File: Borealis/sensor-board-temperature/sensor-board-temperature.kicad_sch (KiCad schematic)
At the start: 5 parts, among them J2 Conn_01x03_Pin (data connecti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, J5 Conn_01x03_Pin (power connect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

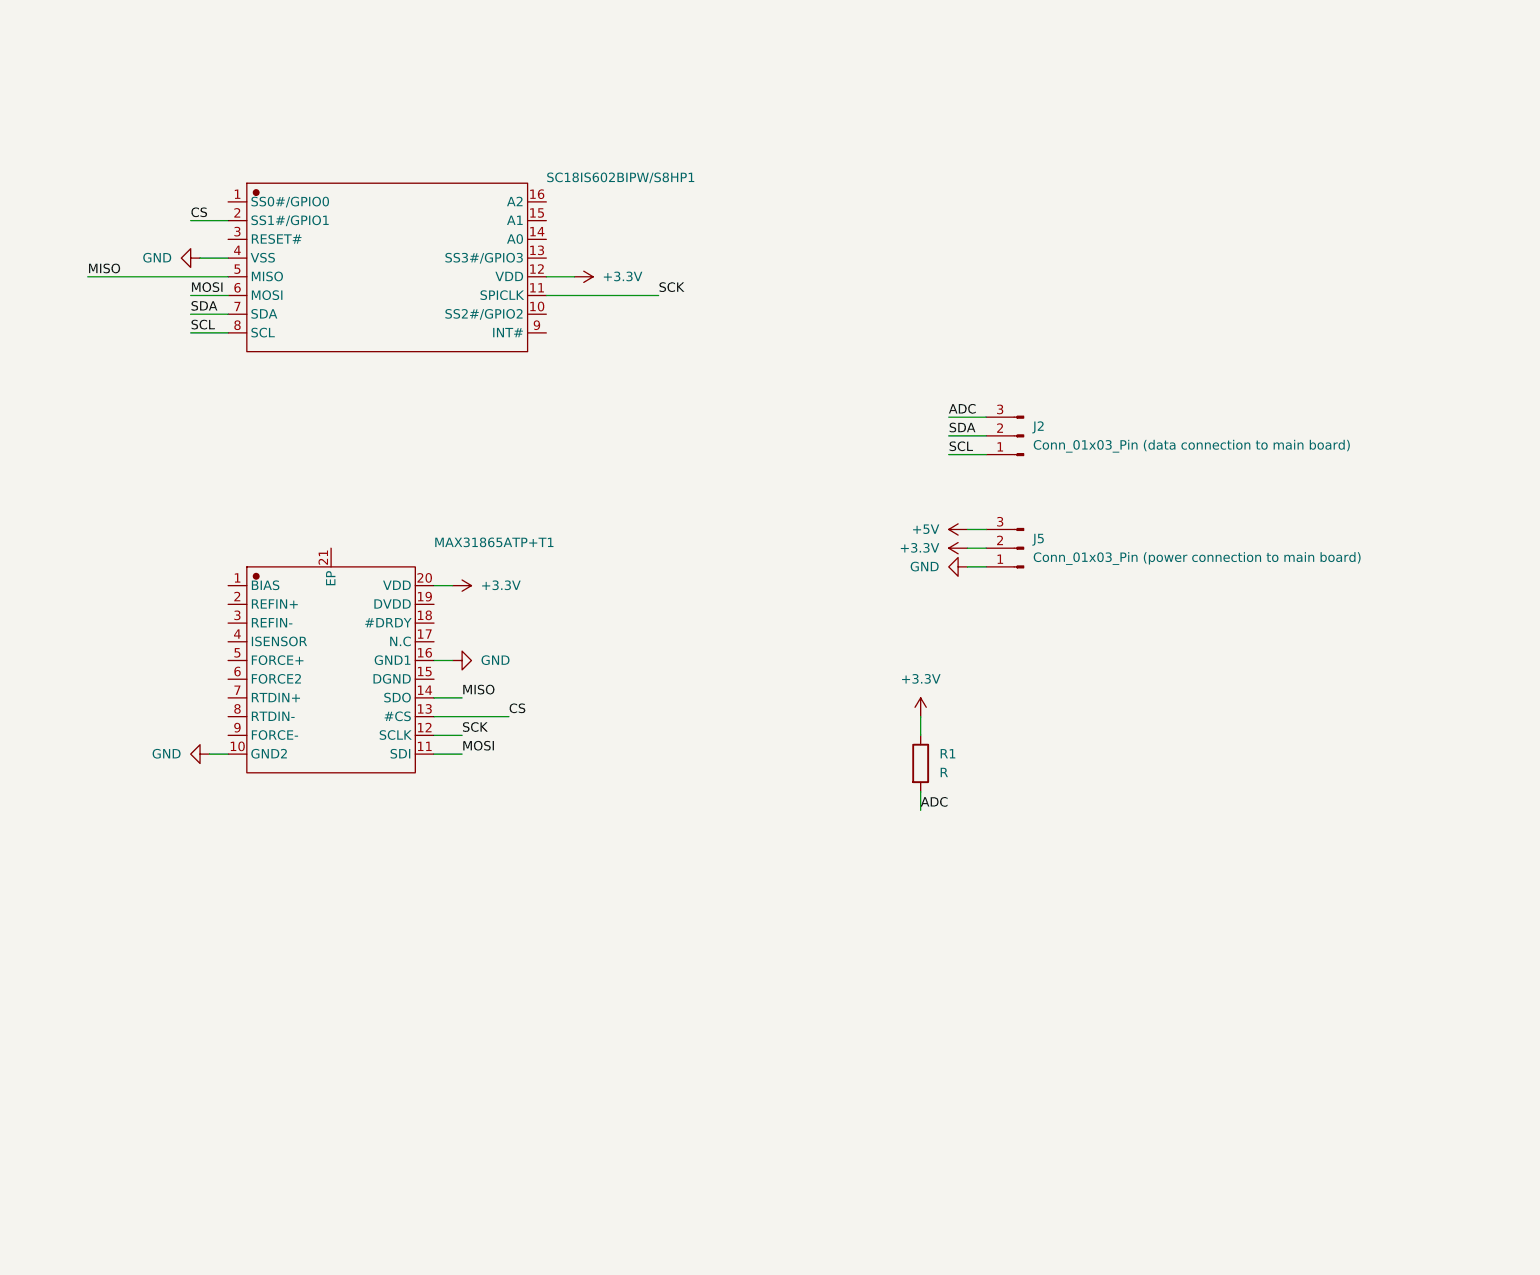
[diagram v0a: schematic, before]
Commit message: Added mainboard and temerature board
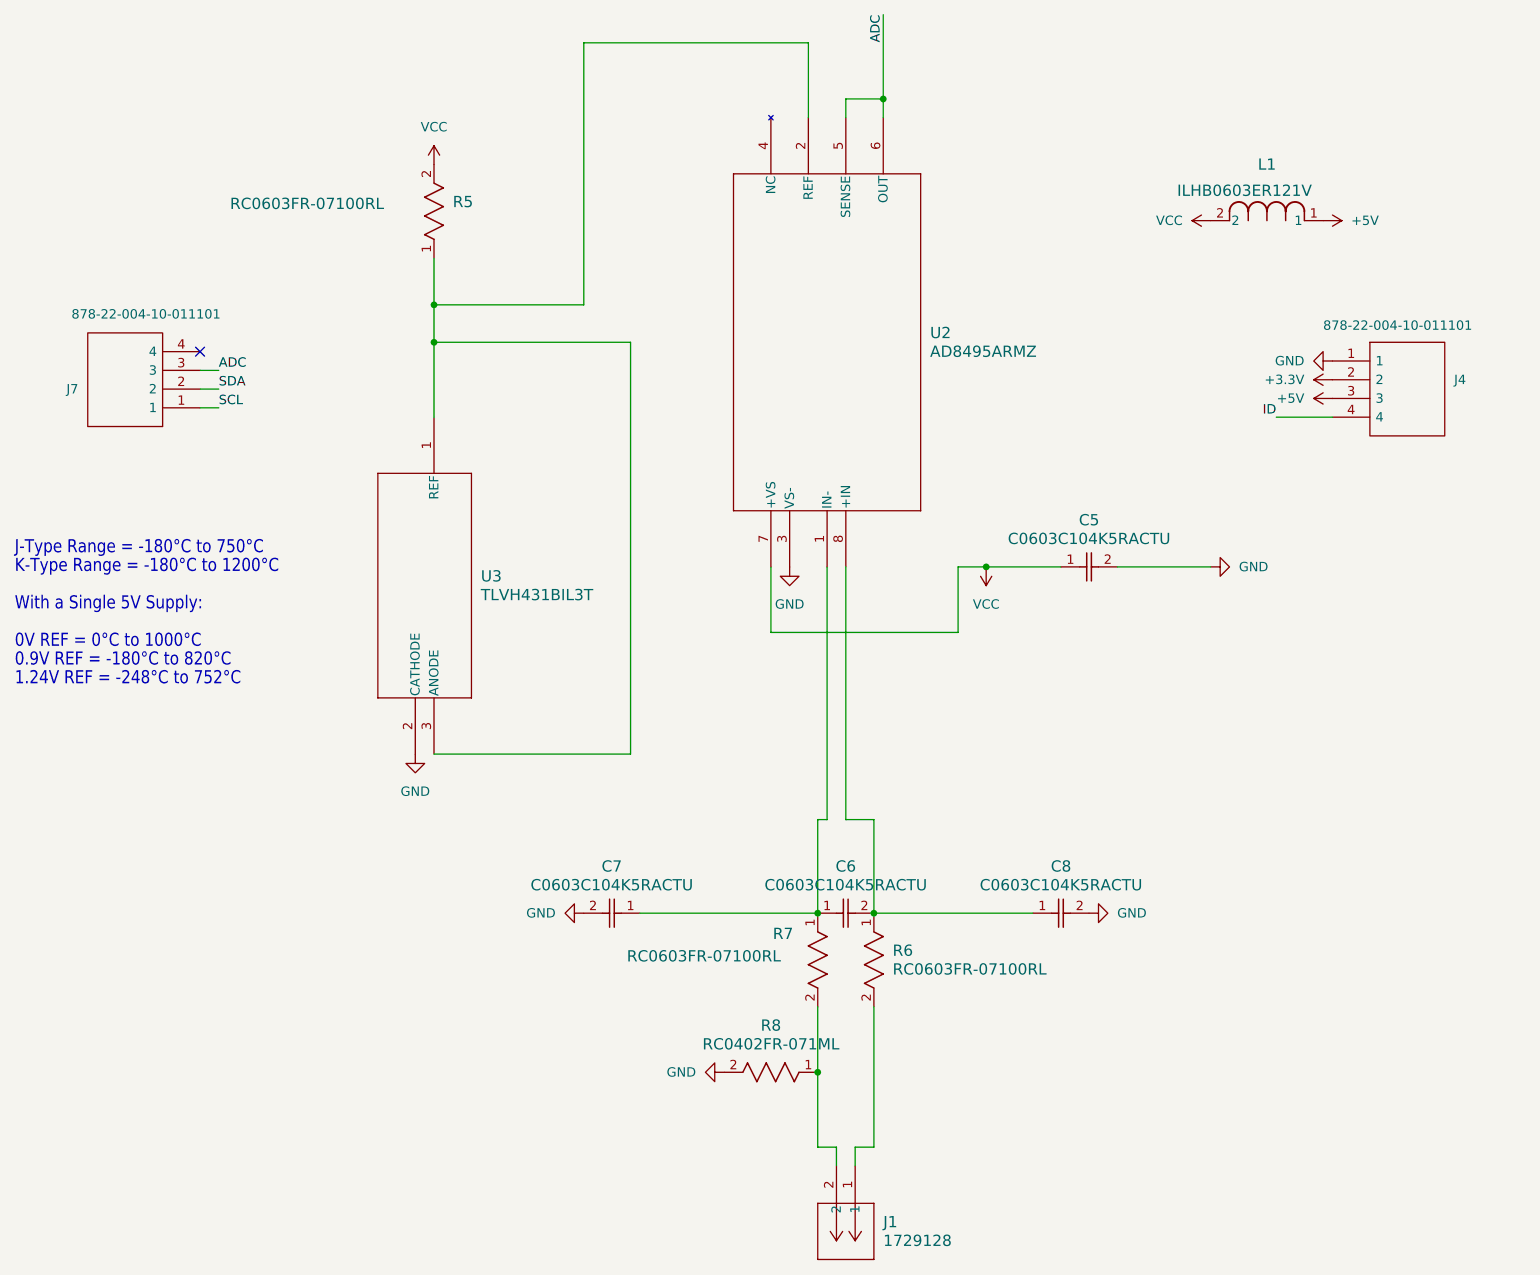
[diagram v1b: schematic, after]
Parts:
- removed J2: Conn_01x03_Pin (data connection to main board), batteryholder:1x03 2.3 pitch, symbol Connector:Conn_01x03_Pin
- removed J5: Conn_01x03_Pin (power connection to main board), batteryholder:1x03 2.3 pitch, symbol Connector:Conn_01x03_Pin
- removed MAX31865ATP+T1: ~, batteryholder:MAX31865ATP+T, symbol MAX31865ATP+T_2025-12-27-altium-import:root_0_MAX31865ATP+T_
- removed R1: R, Resistor_SMD:R_0805_2012Metric, symbol Device:R
- removed SC18IS602BIPW/S8HP1: ~, batteryholder:SC18IS602BIPWS8HP, symbol SC18IS602BIPW-S8HP_2025-12-27-altium-import:root_0_SC18IS602BIPW/S8HP_
- added C5, C6, C7, C8: C0603C104K5RACTU, BOREALIS:CAPC17595_95N_KEM, symbol 2026-01-23_05-30-51:C0603C104K5RACTU
- added J1: 1729128, BOREALIS:CONN_1729128_PXC, symbol 2026-01-23_05-01-15:1729128
- added J4, J7: 878-22-004-10-011101, BOREALIS:8782200410011101, symbol 878-22-004-10-011101:878-22-004-10-011101
- added L1: ILHB0603ER121V, BOREALIS:IND_VISHAY_ILHB0603_VIS, symbol 2026-01-23_05-01-38:ILHB0603ER121V
- added R5, R6, R7: RC0603FR-07100RL, BOREALIS:RC0603N_YAG, symbol 2026-01-23_05-40-00:RC0603FR-07100RL
- added R8: RC0402FR-071ML, BOREALIS:RC0402N_YAG, symbol 2026-01-23_05-51-13:RC0402FR-071ML
- added U2: AD8495ARMZ, BOREALIS:RM_8_ADI, symbol 2026-01-23_05-00-35:AD8495ARMZ
- added U3: TLVH431BIL3T, BOREALIS:SOT23-3-L_3p04x1p4x1p9_STM, symbol 2026-01-23_05-01-00:TLVH431BIL3T
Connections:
- net +3.3V: now also J4.2
- net +5V: now also J4.3, L1.1
- net ADC: now also J7.3, U2.5 (SENSE), U2.6 (OUT)
- net GND: now also C5.2, C7.2, C8.2, J4.1, R8.2, U2.3 (VS-), U3.2 (CATHODE)
- net SCL: now also J7.1
- net SDA: now also J7.2
- new net: R5.1, U2.2 (REF), U3.1 (REF), U3.3 (ANODE)
- new net: C6.1, C7.1, R7.1, U2.1 (IN-)
- new net: C6.2, C8.1, R6.1, U2.8 (+IN)
- new net: J1.2, R7.2, R8.1
- new net: J1.1, R6.2
- new net ID: J4.4
- new net VCC: C5.1, L1.2, R5.2, U2.7 (+VS)
- no-connect marks 0 -> 1
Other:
- note added: "0.9V REF = -180°C to 820°C"
- note added: "0V REF = 0°C to 1000°C"
- note added: "1.24V REF = -248°C to 752°C"
- note added: "J-Type Range = -180°C to 750°C"
- note added: "K-Type Range = -180°C to 1200°C"
- note added: "With a Single 5V Supply:"

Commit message: Fixed a few things
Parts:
- added R1: R, Resistor_SMD:R_0805_2012Metric, symbol Device:R
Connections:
- net +3.3V: now also R1.1
- net ID: now also R1.2
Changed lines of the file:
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@@
+	(wire
+		(pts
+			(xy 212.09 109.22) (xy 212.09 106.68)
+		)
+		(stroke
+			(width 0)
+			(type default)
+		)
+	)
+	(wire
+		(pts
+			(xy 212.09 96.52) (xy 212.09 99.06)
+		)
+		(stroke
+			(width 0)
+			(type default)
+		)
+	)
 	(wire
 		(pts
@@
 		)
 	)
+	(label "ID"
+		(at 212.09 109.22 0)
+		(effects
+			(font
+				(size 1.27 1.27)
+			)
+			(justify left bottom)
+		)
+	)
 	(symbol
 		(lib_id "power:GND")
@@
 	)
 	(symbol
+		(lib_id "power:+3.3V")
+		(at 212.09 96.52 0)
+		(unit 1)
+		(exclude_from_sim no)
+		(in_bom yes)
+		(on_board yes)
+		(dnp no)
+		(fields_autoplaced yes)
+		(property "Reference" "#PWR013"
+			(at 212.09 100.33 0)
+			(effects
+				(font
+					(size 1.27 1.27)
+				)
+				(hide yes)
+			)
+		)
+		(property "Value" "+3.3V"
+			(at 212.09 91.44 0)
+			(effects
+				(font
+					(size 1.27 1.27)
+				)
+			)
+		)
+		(property "Footprint" ""
+			(at 212.09 96.52 0)
+			(effects
+				(font
+					(size 1.27 1.27)
+				)
+				(hide yes)
+			)
+		)
+		(property "Datasheet" ""
+			(at 212.09 96.52 0)
+			(effects
+				(font
+					(size 1.27 1.27)
+				)
+				(hide yes)
+			)
+		)
+		(property "Description" "Power symbol creates a global label with name \"+3.3V\""
+			(at 212.09 96.52 0)
+			(effects
+				(font
+					(size 1.27 1.27)
+				)
+				(hide yes)
+			)
+		)
+		(pin "1"
+		)
+		(instances
+			(project "sensor-board-temperature"
+				(path "/aef02c21-46ab-4606-9d46-fddf3d3f8930"
+					(reference "#PWR013")
+					(unit 1)
+				)
+			)
+		)
+	)
+	(symbol
 		(lib_id "power:+5V")
 		(at 200.66 44.45 270)
@@
 					(unit 1)
 				)
+			)
+		)
+	)
+	(symbol
+		(lib_id "Device:R")
+		(at 212.09 102.87 0)
+		(unit 1)
+		(exclude_from_sim no)
+		(in_bom yes)
+		(on_board yes)
+		(dnp no)
+		(fields_autoplaced yes)
+		(property "Reference" "R1"
+			(at 214.63 101.5999 0)
+			(effects
+				(font
+					(size 1.27 1.27)
+				)
+				(justify left)
+			)
+		)
+		(property "Value" "R"
+			(at 214.63 104.1399 0)
+			(effects
+				(font
+					(size 1.27 1.27)
+				)
+				(justify left)
+			)
+		)
+		(property "Footprint" "Resistor_SMD:R_0805_2012Metric"
+			(at 210.312 102.87 90)
+			(effects
+				(font
+					(size 1.27 1.27)
+				)
+				(hide yes)
+			)
+		)
+		(property "Datasheet" "~"
+			(at 212.09 102.87 0)
+			(effects
+				(font
+					(size 1.27 1.27)
+				)
+				(hide yes)
+			)
+		)
+		(property "Description" "Resistor"
+			(at 212.09 102.87 0)
+			(effects
+				(font
+					(size 1.27 1.27)
+				)
+				(hide yes)
+			)
+		)
+		(pin "2"
+		)
+		(pin "1"
+		)
+		(instances
+			(project "sensor-board-temperature"
+				(path "/aef02c21-46ab-4606-9d46-fddf3d3f8930"
+					(reference "R1")
+					(unit 1)
+				)
